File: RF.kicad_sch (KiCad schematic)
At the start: 35 parts, among them J301 BWSMA-KWE-Z001, J302 BWSMA-KWE-Z001, J303 BWSMA-KWE-Z001, J304 BWSMA-KWE-Z001, J305 BWSMA-KWE-Z001

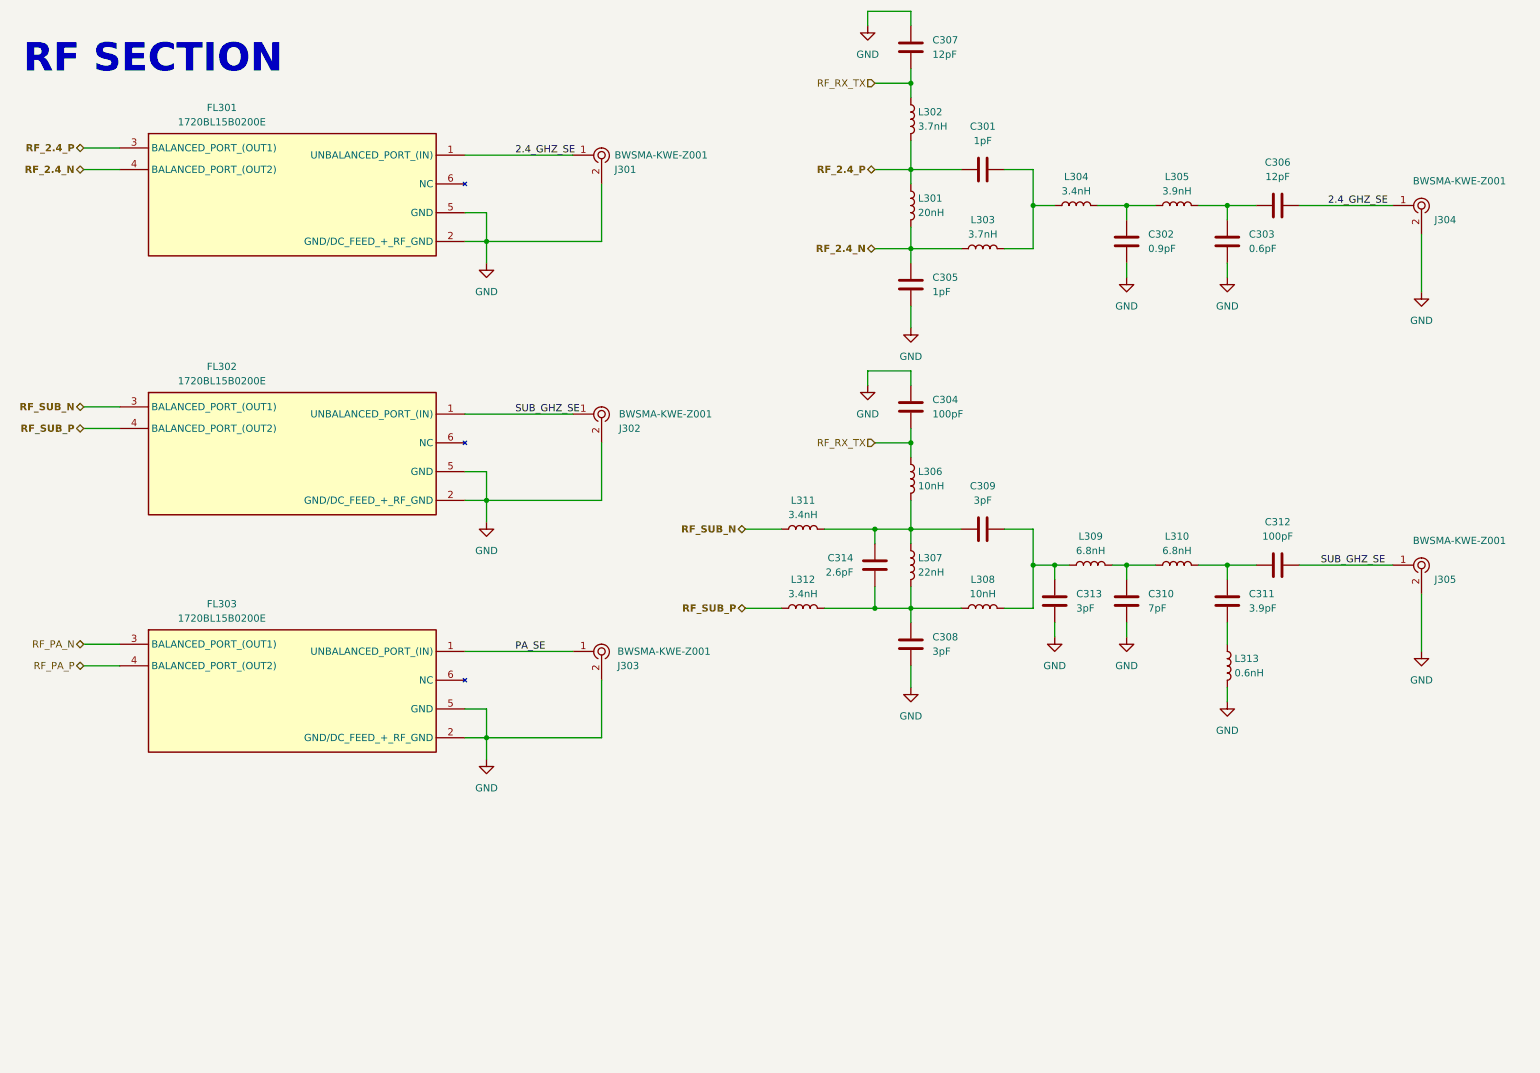
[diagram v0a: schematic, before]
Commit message: replaced baluns with passives & wirewound inductors as recommended, PCB is ready for routing and fencing
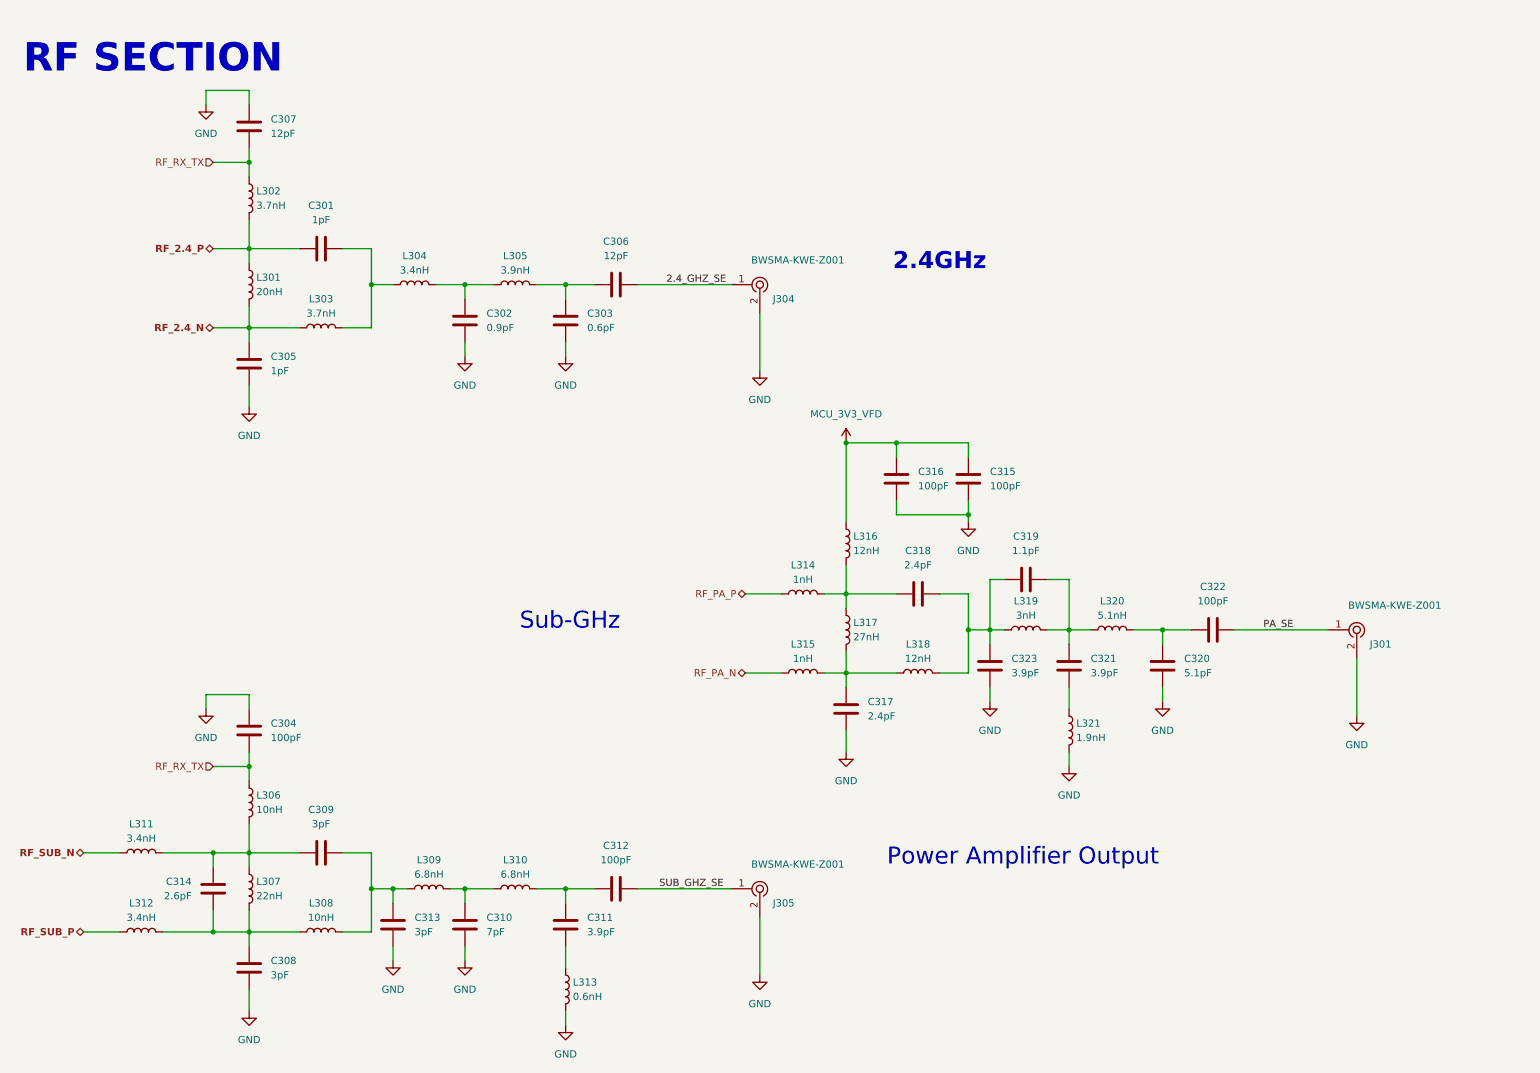
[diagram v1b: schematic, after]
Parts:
- removed FL301, FL302, FL303: 1720BL15B0200E, 1720BL15B0200E:1720BL15B0200E, symbol 1720BL15B0200E:1720BL15B0200E
- removed J302, J303: BWSMA-KWE-Z001, digikey-footprints:RF_SMA_RightAngle_5-1814400-1, symbol dk_Coaxial-Connectors-RF:5-1814400-1
- added C315, C316, C322: 100pF, Capacitor_SMD:C_0402_1005Metric, symbol Device:C
- added C317, C318: 2.4pF, Capacitor_SMD:C_0402_1005Metric, symbol Device:C
- added C319: 1.1pF, Capacitor_SMD:C_0402_1005Metric, symbol Device:C
- added C320: 5.1pF, Capacitor_SMD:C_0402_1005Metric, symbol Device:C
- added C321, C323: 3.9pF, Capacitor_SMD:C_0402_1005Metric, symbol Device:C
- added L314, L315: 1nH, Inductor_SMD:L_0402_1005Metric, symbol Device:L
- added L316, L318: 12nH, Inductor_SMD:L_0402_1005Metric, symbol Device:L
- added L317: 27nH, Inductor_SMD:L_0402_1005Metric, symbol Device:L
- added L319: 3nH, Inductor_SMD:L_0402_1005Metric, symbol Device:L
- added L320: 5.1nH, Inductor_SMD:L_0402_1005Metric, symbol Device:L
- added L321: 1.9nH, Inductor_SMD:L_0402_1005Metric, symbol Device:L
- C301, C302, C303, C304, C305, C306, C307, C308, C309, C310, C311, C312, C313, C314: footprint (none) -> Capacitor_SMD:C_0402_1005Metric
- L301, L302, L303, L304, L305, L306, L307, L308, L309, L310, L311, L312, L313: footprint (none) -> Inductor_SMD:L_0402_1005Metric
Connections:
- net 2.4_GHZ_SE: no longer J301.1
- net GND: now also C315.1, C316.1, C317.1, C320.1, C323.1, L321.2
- net PA_SE: now also J301.1, C322.1
- net RF_PA_N: now also L315.1
- net RF_PA_P: now also L314.1
- new net: C318.2, C319.1, C323.2, L318.2, L319.1
- new net: C319.2, C321.2, L319.2, L320.1
- new net: C320.2, C322.2, L320.2
- new net: C318.1, L314.2, L316.2, L317.1
- new net: C317.2, L315.2, L317.2, L318.1
- new net: C321.1, L321.1
- new net MCU_3V3_VFD: C315.2, C316.2, L316.1
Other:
- note added: "2.4GHz"
- note added: "Power Amplifier Output"
- note added: "Sub-GHz"
- moved on the sheet: C301, C302, C303, C304, C305, C306, C307, C308, C309, C310, C311, C312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
